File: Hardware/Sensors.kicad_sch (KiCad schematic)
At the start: 41 parts, among them U10 W25Q128JVSIQ, U11 SN65HVD230, U12 BMI270, U5 AT7456E, U7 ICM-42688-P, U8 QMC5883P, U9 BMP388, Y1 27Mhz 20pF

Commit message: Added Necessary Connectors, pads and comments in the respective file
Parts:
- renumbered C33 to C40, C36 to C41, C35 to C42, C37 to C43, C30 to C44, C42 to C45, C32 to C46, C48 to C47, C18 to C48, C22 to C49, C24 to C50, C31 to C51, C27 to C52, C28 to C53, C34 to C54, C20 to C55, C21 to C56, C26 to C57, C38 to C58, D5 to D8, R27 to R24, R28 to R25, R29 to R26, R25 to R27, R26 to R28, R22 to R29, R24 to R30, R20 to R31, R21 to R32, R16 to R33, R31 to R34, R30 to R35, U12 to U10, U8 to U11, U5 to U12, U9 to U13, U11 to U14, U7 to U8, U10 to U9, Y1 to Y2

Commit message: Added Digital Airspeed Sensor Connector, Changed the Magnetometer
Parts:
- removed C44: 0.1uF, Capacitor_SMD:C_0402_1005Metric, symbol Device:C_Small
- removed C46: 4.7uF, Capacitor_SMD:C_0603_1608Metric, symbol Device:C_Small
- removed R29, R30: 4.7k, Resistor_SMD:R_0402_1005Metric, symbol Device:R_Small
- removed R33: 0, Resistor_SMD:R_0402_1005Metric, symbol Device:R_Small
- removed U11: QMC5883P, memo:QMC5883P, symbol Magneto:QMC5883P
- added C41, C42: 0.1uF, Capacitor_SMD:C_0402_1005Metric, symbol Device:C_Small
- added C43: 1uF, Capacitor_SMD:C_0402_1005Metric, symbol Device:C_Small
- added U11: LIS3MDLTR, memo:(mag)LGA-12_L2.0-W2.0-P0.50-BL, symbol mag:LIS3MDLTR
- renumbered C40 to C37, C41 to C38, C42 to C39, C43 to C40, C45 to C44, C47 to C45, C48 to C46, C51 to C47, C49 to C48, C50 to C49, C52 to C50, C54 to C51, C53 to C52, C55 to C53, C56 to C54, C57 to C55, C58 to C56, R31 to R29, R32 to R30, R34 to R31, R35 to R32, U13 to U12, U12 to U13
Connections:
- net +3.3V: now also C42.1, C43.1, U11.10 (CS), U11.5 (Vdd), U11.6 (Vdd_IO)
- net GND: now also C41.2, C42.2, C43.2, U11.12 (Res), U11.2 (Res), U11.3 (GND), U11.9 (SD0/SA1)
- net I2C1_SCL: now also U11.1 (SCL/SPC)
- net I2C1_SDA: now also U11.11 (SDA/SDI/SDO)
- new net: C41.1, U11.4 (C1)
- new net MAG_DRDY: U11.8 (DRDY)
- no-connect marks 31 -> 22
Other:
- note added: "only one interrupt is enough,"
- note added: "shares the same bus as Airspeed Sensor One Pull up is sufficient"
- note added: "since it is sharing the same I2C bus with INA226, on pull up is enough. (done in INA226 Schematics)"
- moved on the sheet: C46, C48, C49, C50, C52, C53, C54, C55, R27, R28, R29, R30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

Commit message: removed enable pin resistor in 9V/12V regulator and Layout progress
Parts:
- C41, C42, C43, U11: now not fitted; now left out of the parts list
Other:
- note added: "3) On board magnetometer is cancelled and execluded from board. it is much more stable as an external module paired with GPS or individually."
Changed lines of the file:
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@@
 	(text "1) Crystal Oscillator capacitor Calculation\n   Depends on the specific crystal capacitance\n   and stray capacitance. Take stray capacitance \n   to be 3 - 5 pF.\n "
 		(exclude_from_sim no)
-		(at 552.45 46.736 0)
+		(at 514.604 46.228 0)
 		(effects
 			(font
@@
 				(bold yes)
 			)
+			(justify left)
 		)
 	)
@@
 	(text "2) A)CAN bus requires 120Ω termination resistors\n   at both physical ends of the bus only.\n   If the flight controller is positioned in\n   the middle of the CAN chain, no termination\n   should be installed. Populate R30 only\n   if the flight controller is at one end of the bus.\n\n   B) 0Ω Resistor on RS for slope control,\n      now its configured for High speed. If\n      the wires are long then 10kΩ - 100kΩ \n      should be used\n\n\n "
 		(exclude_from_sim no)
-		(at 552.958 101.092 0)
+		(at 514.096 91.44 0)
 		(effects
 			(font
@@
 				(bold yes)
 			)
+			(justify left)
 		)
 	)
@@
 		)
 	)
+	(text "3) On board magnetometer is cancelled and \n   execluded from board. it is much more stable \n   as an external module paired with GPS \n   or individually. "
+		(exclude_from_sim no)
+		(at 515.874 123.952 0)
+		(effects
+			(font
+				(size 2.032 2.032)
+				(thickness 0.4064)
+				(bold yes)
+			)
+			(justify left)
+		)
+	)
 	(text "OSD"
 		(exclude_from_sim no)
@@
 		(unit 1)
 		(exclude_from_sim no)
-		(in_bom yes)
-		(on_board yes)
-		(dnp no)
+		(in_bom no)
+		(on_board no)
+		(dnp yes)
 		(fields_autoplaced yes)
 		(property "Reference" "U11"
@@
 		(unit 1)
 		(exclude_from_sim no)
-		(in_bom yes)
-		(on_board yes)
-		(dnp no)
+		(in_bom no)
+		(on_board no)
+		(dnp yes)
 		(property "Reference" "C42"
 			(at 171.45 207.01 90)
@@
 		(unit 1)
 		(exclude_from_sim no)
-		(in_bom yes)
-		(on_board yes)
-		(dnp no)
+		(in_bom no)
+		(on_board no)
+		(dnp yes)
 		(property "Reference" "C41"
 			(at 171.45 198.12 90)
@@
 		(unit 1)
 		(exclude_from_sim no)
-		(in_bom yes)
-		(on_board yes)
-		(dnp no)
+		(in_bom no)
+		(on_board no)
+		(dnp yes)
 		(property "Reference" "C43"
 			(at 171.45 215.9 90)

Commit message: Changed to CMOS, layout progress
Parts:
- renumbered C37 to C36, C38 to C37, C39 to C38, C40 to C39, C41 to C40, C42 to C41, C43 to C42, C44 to C43, C45 to C44, C46 to C45, C47 to C46, C48 to C47, C49 to C48, C50 to C49, C51 to C50, C52 to C51, C53 to C52, C54 to C53, C55 to C54, C56 to C55, R23 to R19, R24 to R20, R25 to R21, R26 to R22, R27 to R23, R28 to R24, R29 to R25, R30 to R26, R31 to R27, R32 to R28

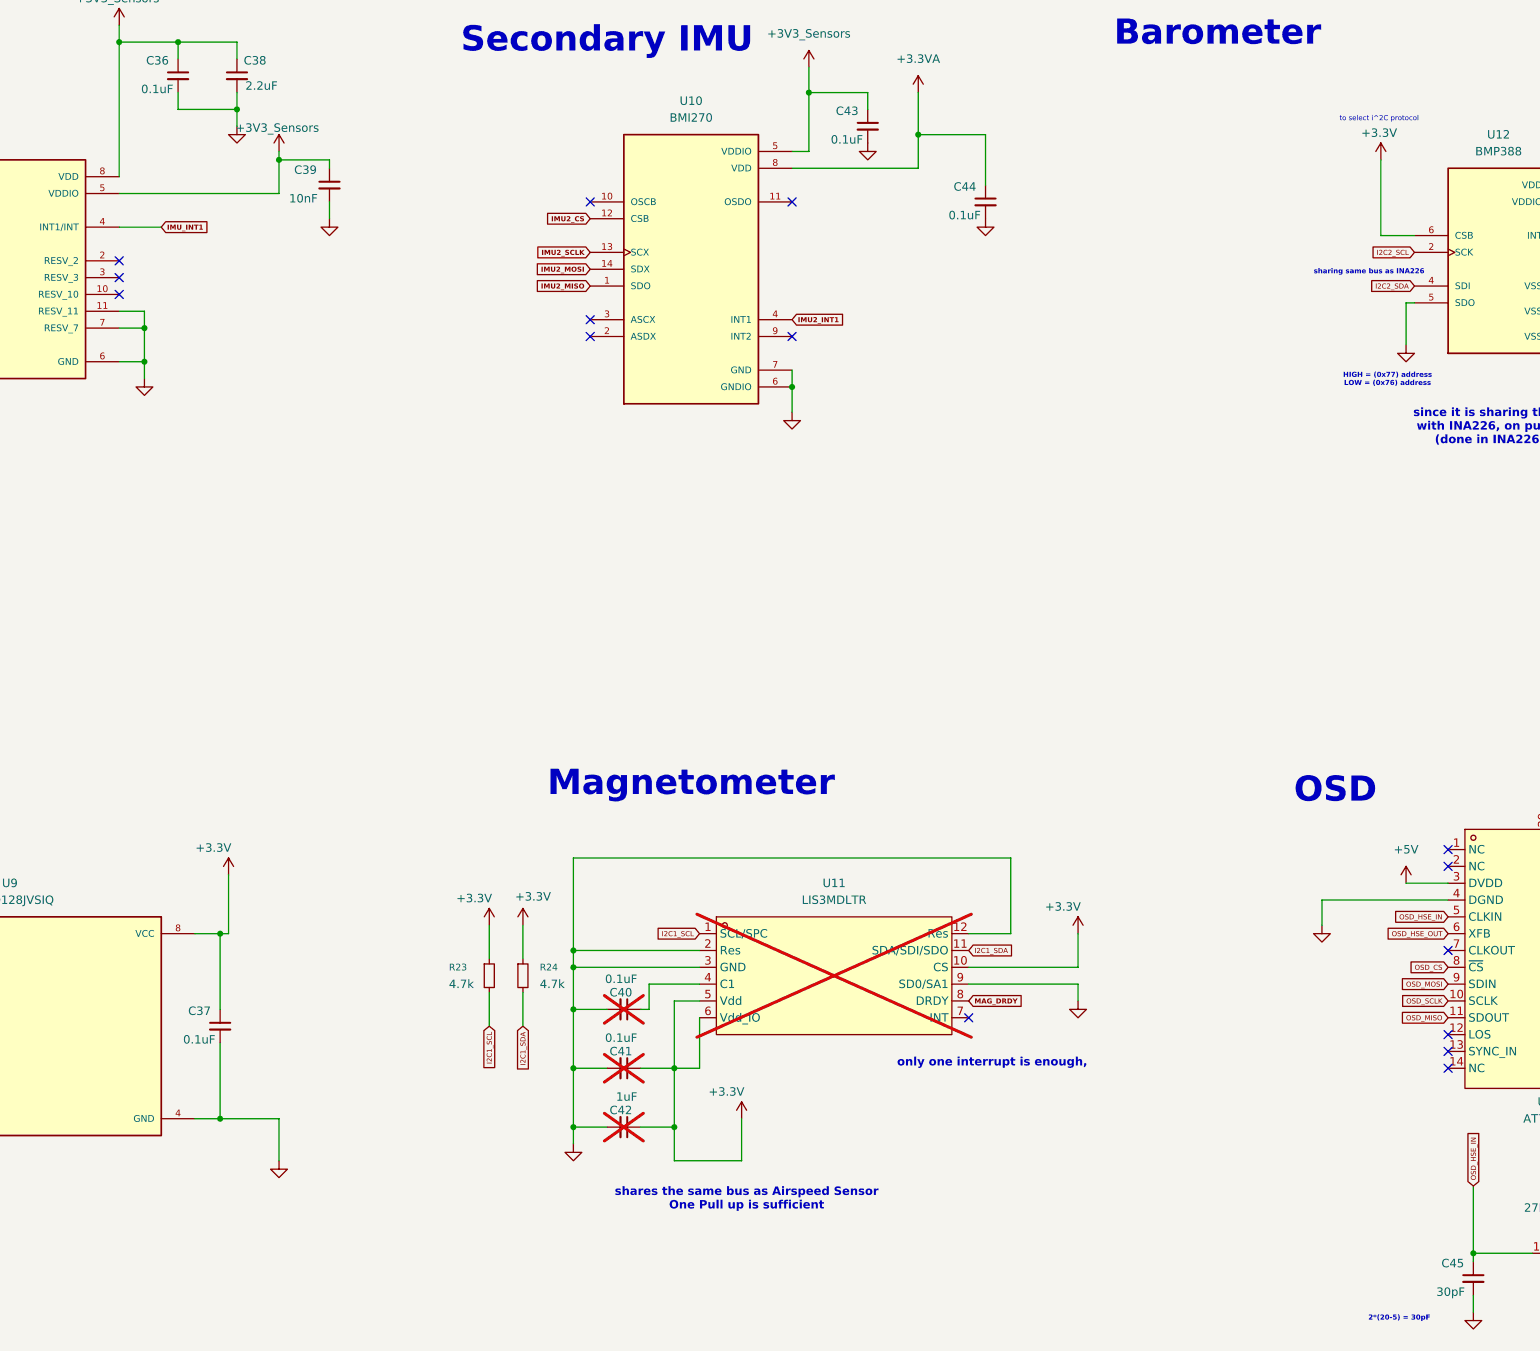
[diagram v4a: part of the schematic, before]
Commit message: added firmware drivers for all sensors for the test board
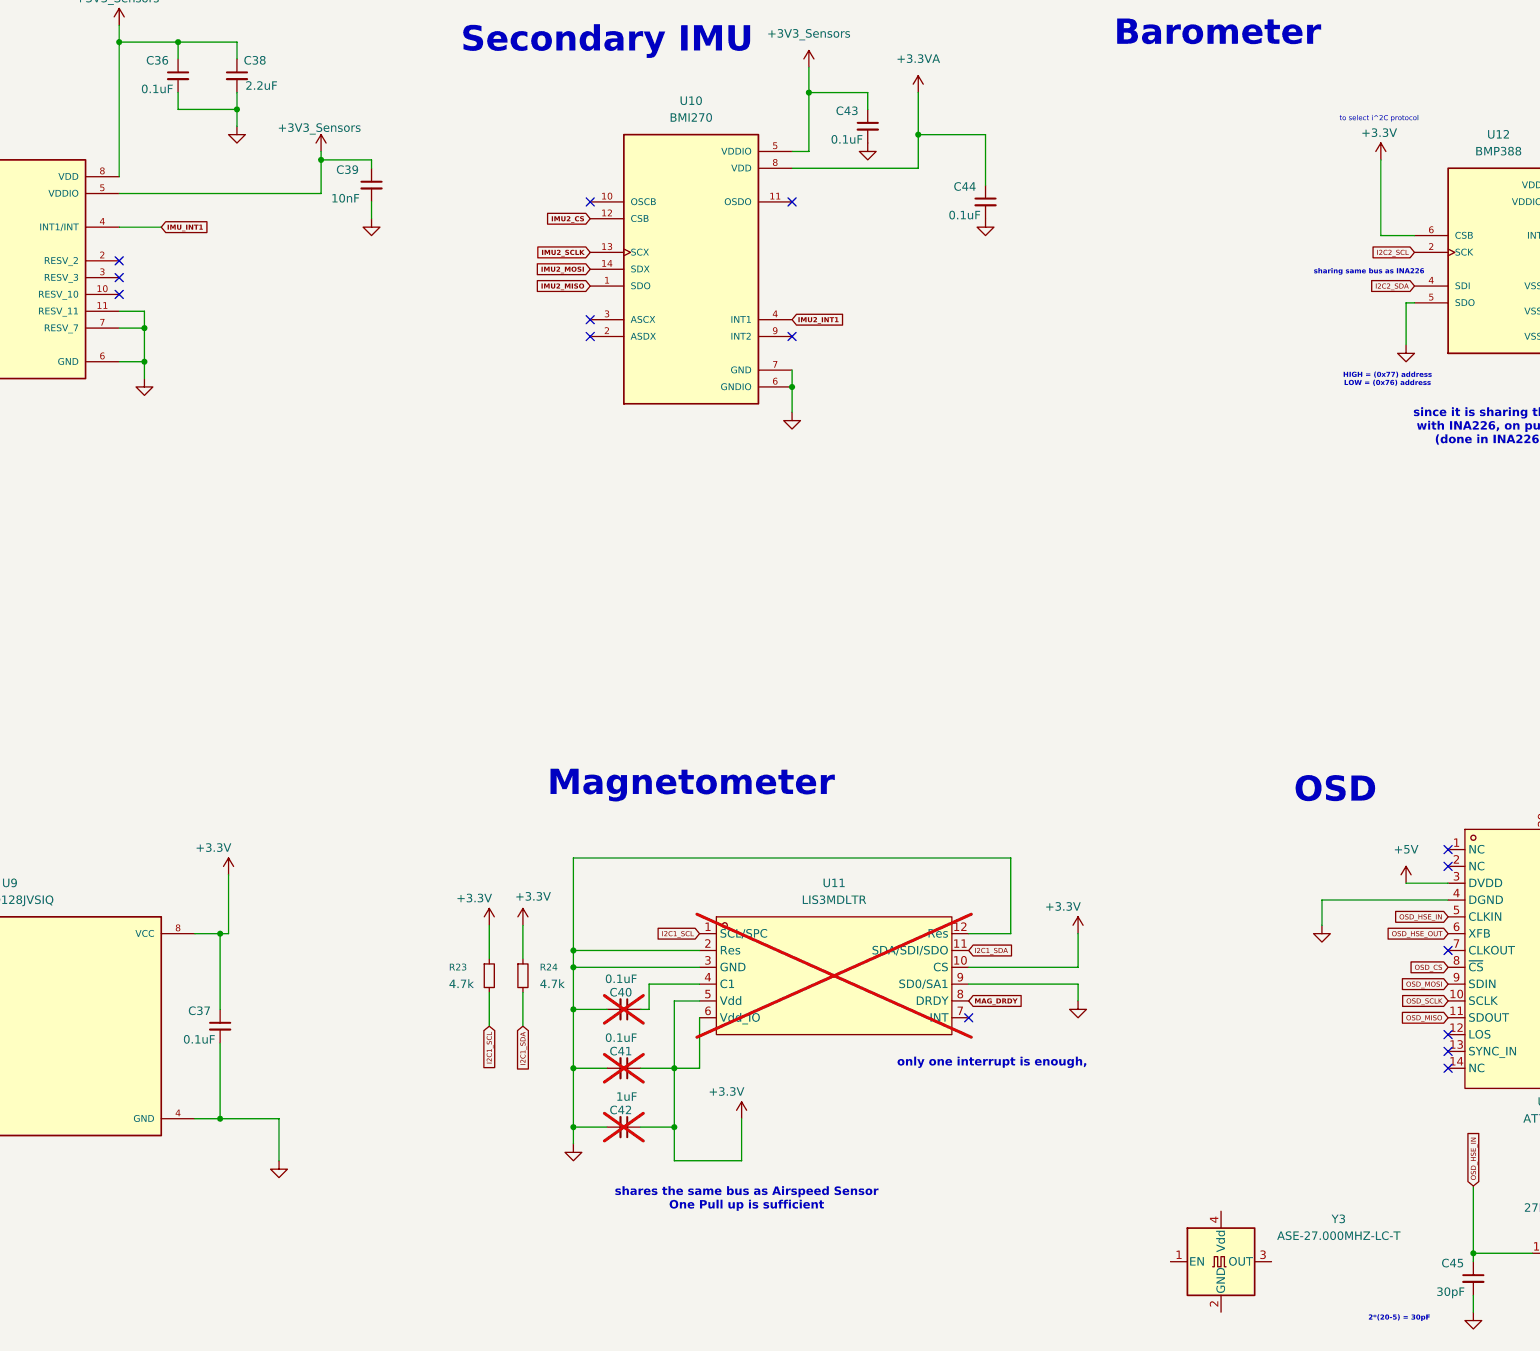
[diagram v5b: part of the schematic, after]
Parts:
- added Y3: ASE-27.000MHZ-LC-T, Oscillator:Oscillator_SMD_Abracon_ASE-4Pin_3.2x2.5mm, symbol Oscillator:ASE-xxxMHz
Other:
- moved on the sheet: C39
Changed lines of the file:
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@@
 	)
 	(junction
-		(at 118.11 72.39)
+		(at 124.46 72.39)
 		(diameter 0)
 		(color 0 0 0 0)
@@
 	(wire
 		(pts
-			(xy 125.73 73.66) (xy 125.73 72.39)
+			(xy 132.08 73.66) (xy 132.08 72.39)
 		)
 		(stroke
@@
 	(wire
 		(pts
-			(xy 93.98 77.47) (xy 118.11 77.47)
+			(xy 93.98 77.47) (xy 124.46 77.47)
 		)
 		(stroke
@@
 	(wire
 		(pts
-			(xy 118.11 71.12) (xy 118.11 72.39)
+			(xy 124.46 71.12) (xy 124.46 72.39)
 		)
 		(stroke
@@
 	(wire
 		(pts
-			(xy 125.73 72.39) (xy 118.11 72.39)
+			(xy 132.08 72.39) (xy 124.46 72.39)
 		)
 		(stroke
@@
 	(wire
 		(pts
-			(xy 125.73 81.28) (xy 125.73 78.74)
+			(xy 132.08 81.28) (xy 132.08 78.74)
 		)
 		(stroke
@@
 	(wire
 		(pts
-			(xy 118.11 72.39) (xy 118.11 77.47)
+			(xy 124.46 72.39) (xy 124.46 77.47)
 		)
 		(stroke
@@
 	(symbol
 		(lib_id "Device:C_Small")
-		(at 125.73 76.2 0)
+		(at 132.08 76.2 0)
 		(unit 1)
 		(exclude_from_sim no)
@@
 		(dnp no)
 		(property "Reference" "C39"
-			(at 120.396 73.914 0)
+			(at 126.746 73.914 0)
 			(effects
 				(font
@@
 		)
 		(property "Value" "10nF"
-			(at 119.634 78.232 0)
+			(at 125.984 78.232 0)
 			(effects
 				(font
@@
 		)
 		(property "Footprint" "Capacitor_SMD:C_0402_1005Metric"
-			(at 125.73 76.2 0)
+			(at 132.08 76.2 0)
 			(effects
 				(font
@@
 		)
 		(property "Datasheet" "~"
-			(at 125.73 76.2 0)
+			(at 132.08 76.2 0)
 			(effects
 				(font
@@
 		)
 		(property "Description" "Unpolarized capacitor, small symbol"
-			(at 125.73 76.2 0)
+			(at 132.08 76.2 0)
 			(effects
 				(font
@@
 	(symbol
 		(lib_id "power:+3.3V")
-		(at 118.11 71.12 0)
+		(at 124.46 71.12 0)
 		(unit 1)
 		(exclude_from_sim no)
@@
 		(dnp no)
 		(property "Reference" "#PWR074"
-			(at 118.11 74.93 0)
+			(at 124.46 74.93 0)
 			(effects
 				(font
@@
 		)
 		(property "Value" "+3V3_Sensors"
-			(at 117.856 67.564 0)
+			(at 124.206 67.564 0)
 			(effects
 				(font
@@
 		)
 		(property "Footprint" ""
-			(at 118.11 71.12 0)
+			(at 124.46 71.12 0)
 			(effects
 				(font
@@
 		)
 		(property "Datasheet" ""
-			(at 118.11 71.12 0)
+			(at 124.46 71.12 0)
 			(effects
 				(font
@@
 		)
 		(property "Description" "Power symbol creates a global label with name \"+3.3V\""
-			(at 118.11 71.12 0)
+			(at 124.46 71.12 0)
 			(effects
 				(font
@@
 	(symbol
 		(lib_id "power:GND")
-		(at 125.73 81.28 0)
+		(at 132.08 81.28 0)
 		(unit 1)
 		(exclude_from_sim no)
@@
 		(fields_autoplaced yes)
 		(property "Reference" "#PWR076"
-			(at 125.73 87.63 0)
+			(at 132.08 87.63 0)
 			(effects
 				(font
@@
 		)
 		(property "Value" "GND"
-			(at 125.73 86.36 0)
+			(at 132.08 86.36 0)
 			(effects
 				(font
@@
 		)
 		(property "Footprint" ""
-			(at 125.73 81.28 0)
+			(at 132.08 81.28 0)
 			(effects
 				(font
@@
 		)
 		(property "Datasheet" ""
-			(at 125.73 81.28 0)
+			(at 132.08 81.28 0)
 			(effects
 				(font
@@
 		)
 		(property "Description" "Power symbol creates a global label with name \"GND\" , ground"
-			(at 125.73 81.28 0)
+			(at 132.08 81.28 0)
 			(effects
 				(font
@@
 					(unit 1)
 				)
+			)
+		)
+	)
+	(symbol
+		(lib_id "Oscillator:ASE-xxxMHz")
+		(at 260.35 238.76 0)
+		(unit 1)
+		(exclude_from_sim no)
+		(in_bom yes)
+		(on_board yes)
+		(dnp no)
+		(fields_autoplaced yes)
+		(property "Reference" "Y3"
+			(at 278.13 232.3398 0)
+			(effects
+				(font
+					(size 1.27 1.27)
+				)
+			)
+		)
+		(property "Value" "ASE-27.000MHZ-LC-T"
+			(at 278.13 234.8798 0)
+			(effects
+				(font
+					(size 1.27 1.27)
+				)
+			)
+		)
+		(property "Footprint" "Oscillator:Oscillator_SMD_Abracon_ASE-4Pin_3.2x2.5mm"
+			(at 278.13 247.65 0)
+			(effects
+				(font
+					(size 1.27 1.27)
+				)
+				(hide yes)
+			)
+		)
+		(property "Datasheet" "http://www.abracon.com/Oscillators/ASV.pdf"
+			(at 257.81 238.76 0)
+			(effects
+				(font
+					(size 1.27 1.27)
+				)
+				(hide yes)
+			)
+		)
+		(property "Description" "3.3V CMOS SMD Crystal Clock Oscillator, Abracon"
+			(at 260.35 238.76 0)
+			(effects
+				(font
+					(size 1.27 1.27)
+				)
+				(hide yes)
+			)
+		)
+		(pin "2"
+		)
+		(pin "1"
+		)
+		(pin "4"
+		)
+		(pin "3"
+		)
+		(instances
+			(project "Flight Controller"
+				(path "/affbaa1c-796a-43e2-b357-d8056264fe45/cba678f1-cd76-4d72-9114-2cc1e511120c"
+					(reference "Y3")
+					(unit 1)
+				)

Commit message: progress layout
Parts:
- C45, C47: footprint Capacitor_SMD:C_0603_1608Metric -> Capacitor_SMD:C_0402_1005Metric
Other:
- moved on the sheet: Y3
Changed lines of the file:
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@@
 			)
 		)
-		(property "Footprint" "Capacitor_SMD:C_0603_1608Metric"
+		(property "Footprint" "Capacitor_SMD:C_0402_1005Metric"
 			(at 298.45 241.3 0)
 			(effects
@@
 			)
 		)
-		(property "Footprint" "Capacitor_SMD:C_0603_1608Metric"
+		(property "Footprint" "Capacitor_SMD:C_0402_1005Metric"
 			(at 323.85 241.3 0)
 			(effects
@@
 	(symbol
 		(lib_id "Oscillator:ASE-xxxMHz")
-		(at 260.35 238.76 0)
+		(at 237.49 241.3 0)
 		(unit 1)
 		(exclude_from_sim no)
@@
 		(fields_autoplaced yes)
 		(property "Reference" "Y3"
-			(at 278.13 232.3398 0)
+			(at 255.27 234.8798 0)
 			(effects
 				(font
@@
 		)
 		(property "Value" "ASE-27.000MHZ-LC-T"
-			(at 278.13 234.8798 0)
+			(at 255.27 237.4198 0)
 			(effects
 				(font
@@
 		)
 		(property "Footprint" "Oscillator:Oscillator_SMD_Abracon_ASE-4Pin_3.2x2.5mm"
-			(at 278.13 247.65 0)
+			(at 255.27 250.19 0)
 			(effects
 				(font
@@
 		)
 		(property "Datasheet" "http://www.abracon.com/Oscillators/ASV.pdf"
-			(at 257.81 238.76 0)
+			(at 234.95 241.3 0)
 			(effects
 				(font
@@
 		)
 		(property "Description" "3.3V CMOS SMD Crystal Clock Oscillator, Abracon"
-			(at 260.35 238.76 0)
+			(at 237.49 241.3 0)
 			(effects
 				(font

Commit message: changed hella stuff in firmware plan and hardware pcb layout
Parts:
- removed Y3: ASE-27.000MHZ-LC-T, Oscillator:Oscillator_SMD_Abracon_ASE-4Pin_3.2x2.5mm, symbol Oscillator:ASE-xxxMHz
- added R29, R30: 10k, Resistor_SMD:R_0402_1005Metric, symbol Device:R_Small
- C37, C43, C44, C51, C52, C53, C54: footprint Capacitor_SMD:C_0603_1608Metric -> Capacitor_SMD:C_0402_1005Metric
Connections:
- net +3.3VA is gone; now on net +3V3_Sensors: C44.1, U10.8 (VDD)
- net +3.3V: now also R29.2, R30.2
- net I2C2_SCL: now also R30.1
- net I2C2_SDA: now also R29.1
- net MAG_DRDY: no longer names the net of U11.8 (DRDY)
- no-connect marks 22 -> 23

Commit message: hella shit configured, layout progress
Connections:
- net IMU2_CS: now also U8.12 (AP_CS); no longer U10.12 (CSB)
- net IMU2_INT1: now also U8.4 (INT1/INT); no longer U10.4 (INT1)
- net IMU2_MISO: now also U8.1 (AP_SDO/AP_AD0); no longer U10.1 (SDO)
- net IMU2_MOSI: now also U8.14 (AP_SDA/AP_SDIO/AP_SDI); no longer U10.14 (SDX)
- net IMU2_SCLK: now also U8.13 (AP_SCL/AP_SCLK); no longer U10.13 (SCX)
- net IMU_CS: now also U10.12 (CSB); no longer U8.12 (AP_CS)
- net IMU_INT1: now also U10.4 (INT1); no longer U8.4 (INT1/INT)
- net IMU_MISO: now also U10.1 (SDO); no longer U8.1 (AP_SDO/AP_AD0)
- net IMU_MOSI: now also U10.14 (SDX); no longer U8.14 (AP_SDA/AP_SDIO/AP_SDI)
- net IMU_SCLK: now also U10.13 (SCX); no longer U8.13 (AP_SCL/AP_SCLK)
- net CANH renamed CAN_P
- net CANL renamed CAN_N
